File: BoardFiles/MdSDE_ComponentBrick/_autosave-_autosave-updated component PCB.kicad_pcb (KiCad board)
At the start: 2 copper layers, 50 parts, among them P101 CONN_01X10, P102 CONN_01X10, SW201 Coded_Switch, SW202 SPST_x3, SW301 Coded_Switch, SW302 SPST_x3, SW401 Coded_Switch, SW402 SPST_x3, SW501 Coded_Switch, SW502 SPST_x3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

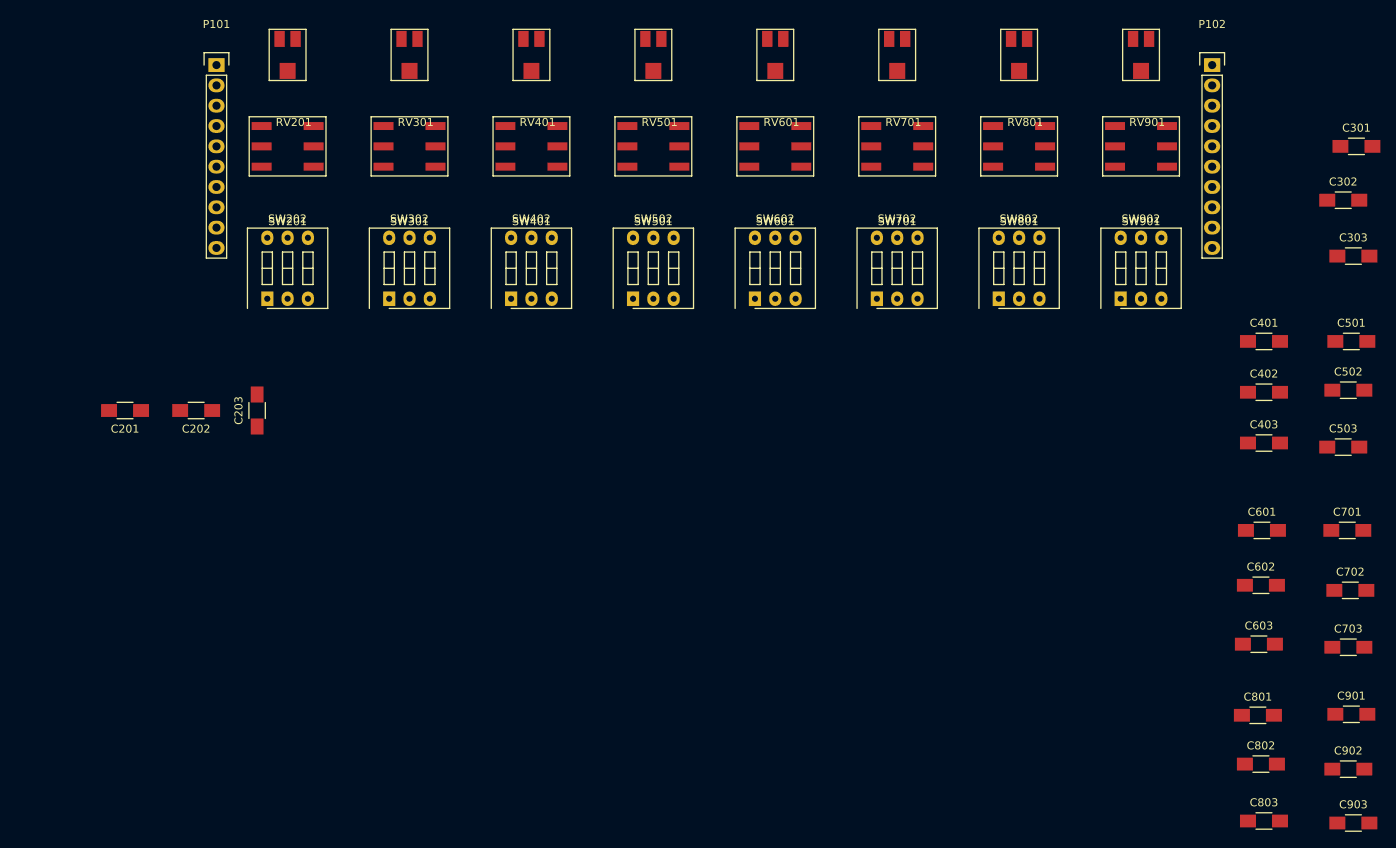
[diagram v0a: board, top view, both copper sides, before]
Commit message: correct spacing for pcb
pre-traced component pcb with correct dimensions
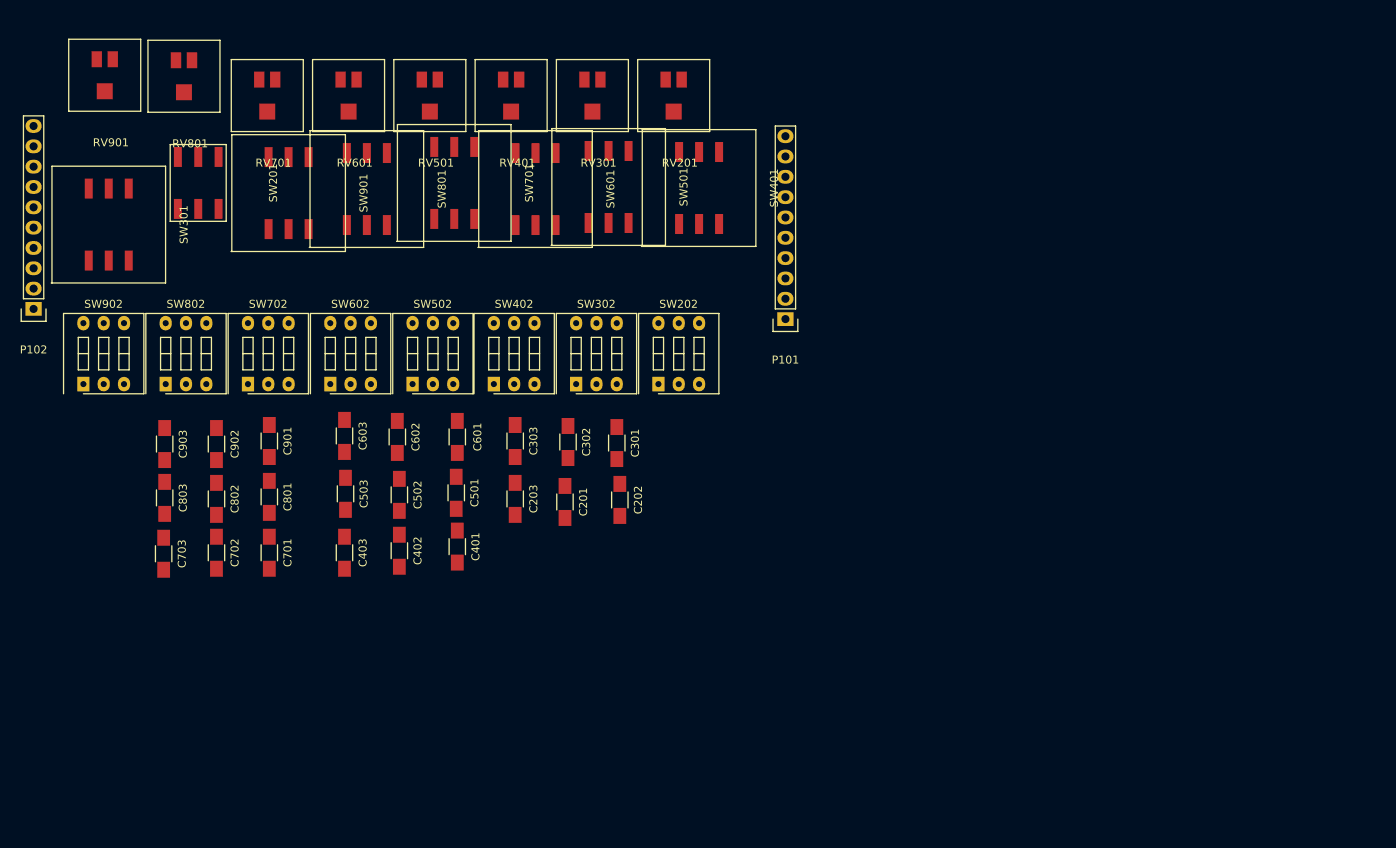
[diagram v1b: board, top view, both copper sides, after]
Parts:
- SW201: footprint Footprints:SH-7000RotarySwitch -> SH-7000RotarySwitch
- moved C903 156.0 mm to (71.0, 117.2), turned to 270 degrees
- moved P102 150.4 mm to (54.6, 100.3), turned to 180 degrees
- moved C703 148.5 mm to (70.9, 130.9), turned to 270 degrees
- moved C902 147.2 mm to (77.5, 117.2), turned to 270 degrees
- moved C803 143.2 mm to (71.0, 124.0), turned to 270 degrees
- moved C702 141.8 mm to (77.5, 130.8), turned to 270 degrees
- moved C901 139.5 mm to (84.1, 116.8), turned to 270 degrees
- moved C701 134.8 mm to (84.1, 130.8), turned to 270 degrees
- moved C802 134.7 mm to (77.5, 124.1), turned to 270 degrees
- moved SW902 130.1 mm to (60.8, 109.7)
- moved RV901 129.6 mm to (63.5, 71.1)
- moved C801 126.6 mm to (84.1, 123.8), turned to 270 degrees
- moved C503 124.9 mm to (93.6, 123.4), turned to 270 degrees
- moved C502 119.3 mm to (100.3, 123.6), turned to 270 degrees
- moved C603 117.2 mm to (93.5, 116.2), turned to 270 degrees
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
